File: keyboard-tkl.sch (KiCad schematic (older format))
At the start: 108 parts, among them P1 USB_OTG, P2 JTAG, U1 AT32UC3B1512, U2 74HC595, U3 74HC595, U4 74HC595, U5 LD1117S33CTR, Y1 12MHz

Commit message: Add stabs to big keys
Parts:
- added SW1, SW2, SW3, SW4, SW5, SW6: MX, mx1a:MXST, symbol MX
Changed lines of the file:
@@
 Wire Wire Line
 	10750 950  10750 1150
+$Comp
+L MX SW3
+U 1 1 55E28F84
+P 2450 2900
+F 0 "SW3" H 2450 2950 60  0000 C CNN
+F 1 "MX" H 2450 2850 60  0000 C CNN
+F 2 "mx1a:MXST" H 2450 2900 60  0000 C CNN
+F 3 "" H 2450 2900 60  0000 C CNN
+	1    2450 2900
+	1    0    0    -1
+$EndComp
+$Comp
+L MX SW4
+U 1 1 55E296F8
+P 4550 2900
+F 0 "SW4" H 4550 2950 60  0000 C CNN
+F 1 "MX" H 4550 2850 60  0000 C CNN
+F 2 "mx1a:MXST" H 4550 2900 60  0000 C CNN
+F 3 "" H 4550 2900 60  0000 C CNN
+	1    4550 2900
+	1    0    0    -1
+$EndComp
+$Comp
+L MX SW6
+U 1 1 55E29E84
+P 6150 2500
+F 0 "SW6" H 6150 2550 60  0000 C CNN
+F 1 "MX" H 6150 2450 60  0000 C CNN
+F 2 "mx1a:MXST" H 6150 2500 60  0000 C CNN
+F 3 "" H 6150 2500 60  0000 C CNN
+	1    6150 2500
+	1    0    0    -1
+$EndComp
+$Comp
+L MX SW5
+U 1 1 55E2A005
+P 5750 2500
+F 0 "SW5" H 5750 2550 60  0000 C CNN
+F 1 "MX" H 5750 2450 60  0000 C CNN
+F 2 "mx1a:MXST" H 5750 2500 60  0000 C CNN
+F 3 "" H 5750 2500 60  0000 C CNN
+	1    5750 2500
+	1    0    0    -1
+$EndComp
+$Comp
+L MX SW1
+U 1 1 55E2A3B8
+P 1150 2500
+F 0 "SW1" H 1150 2550 60  0000 C CNN
+F 1 "MX" H 1150 2450 60  0000 C CNN
+F 2 "mx1a:MXST" H 1150 2500 60  0000 C CNN
+F 3 "" H 1150 2500 60  0000 C CNN
+	1    1150 2500
+	1    0    0    -1
+$EndComp
+$Comp
+L MX SW2
+U 1 1 55E2A529
+P 1300 2500
+F 0 "SW2" H 1300 2550 60  0000 C CNN
+F 1 "MX" H 1300 2450 60  0000 C CNN
+F 2 "mx1a:MXST" H 1300 2500 60  0000 C CNN
+F 3 "" H 1300 2500 60  0000 C CNN
+	1    1300 2500
+	1    0    0    -1
+$EndComp
 $EndSCHEMATC

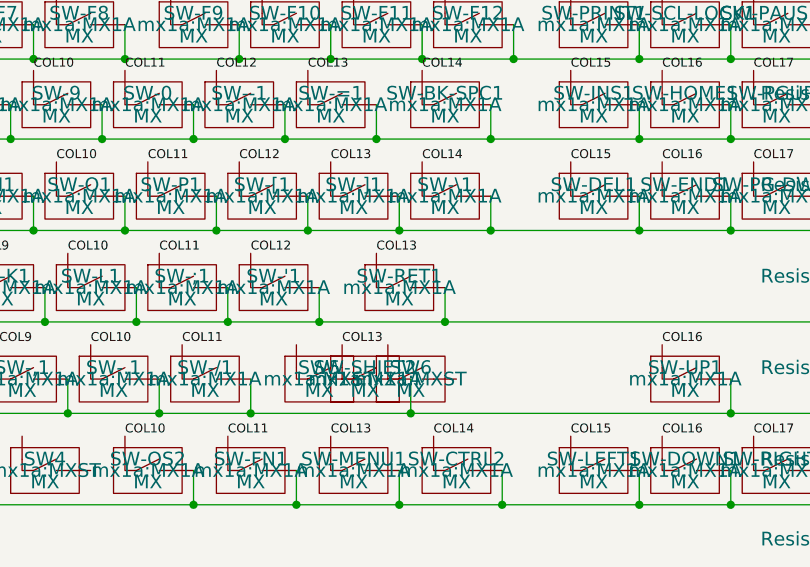
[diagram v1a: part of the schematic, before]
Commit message: Stabilizers placed and spaced
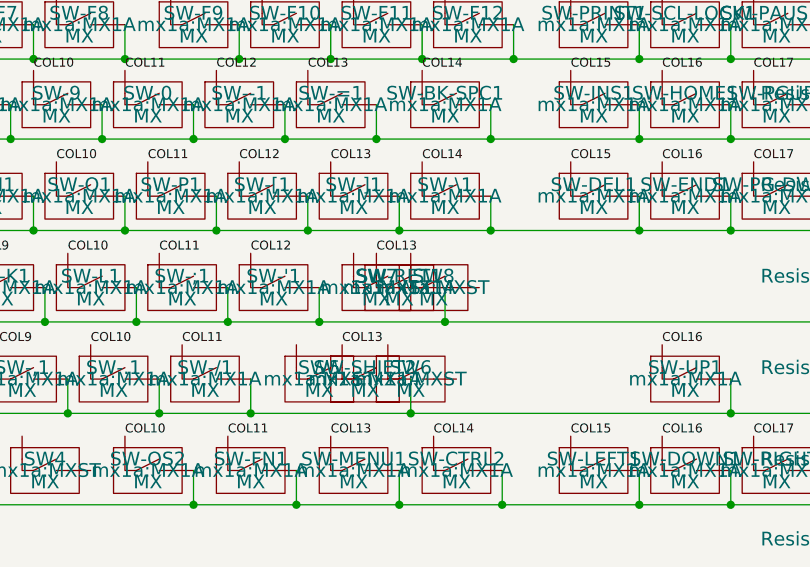
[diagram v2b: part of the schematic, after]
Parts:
- added SW7, SW8: MX, mx1a:MXST, symbol MX
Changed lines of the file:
@@
 $EndComp
 $Comp
-L +3.3V #PWR01
+L +3.3V #PWR2
 U 1 1 55DB292A
 P 2000 4150
-F 0 "#PWR01" H 2000 4000 50  0001 C CNN
+F 0 "#PWR2" H 2000 4000 50  0001 C CNN
 F 1 "+3.3V" H 2000 4290 50  0000 C CNN
 F 2 "" H 2000 4150 60  0000 C CNN
@@
 $EndComp
 $Comp
-L GND #PWR02
+L GND #PWR13
 U 1 1 55DC815B
 P 10800 6300
-F 0 "#PWR02" H 10800 6050 50  0001 C CNN
+F 0 "#PWR13" H 10800 6050 50  0001 C CNN
 F 1 "GND" H 10800 6150 50  0000 C CNN
 F 2 "" H 10800 6300 60  0000 C CNN
@@
 VDDOUT
 $Comp
-L GND #PWR03
+L GND #PWR16
 U 1 1 55DE1148
 P 12250 1450
-F 0 "#PWR03" H 12250 1200 50  0001 C CNN
+F 0 "#PWR16" H 12250 1200 50  0001 C CNN
 F 1 "GND" H 12250 1300 50  0000 C CNN
 F 2 "" H 12250 1450 60  0000 C CNN
@@
 $EndComp
 $Comp
-L +5V #PWR04
+L +5V #PWR15
 U 1 1 55DE1F1A
 P 11550 1400
-F 0 "#PWR04" H 11550 1250 50  0001 C CNN
+F 0 "#PWR15" H 11550 1250 50  0001 C CNN
 F 1 "+5V" H 11550 1540 50  0000 C CNN
 F 2 "" H 11550 1400 60  0000 C CNN
@@
 USB_ID
 $Comp
-L GND #PWR05
+L GND #PWR3
 U 1 1 55DEC1DC
 P 2200 8250
-F 0 "#PWR05" H 2200 8000 50  0001 C CNN
+F 0 "#PWR3" H 2200 8000 50  0001 C CNN
 F 1 "GND" H 2200 8100 50  0000 C CNN
 F 2 "" H 2200 8250 60  0000 C CNN
@@
 $EndComp
 $Comp
-L GND #PWR06
+L GND #PWR8
 U 1 1 55DF2FDE
 P 10050 6250
-F 0 "#PWR06" H 10050 6000 50  0001 C CNN
+F 0 "#PWR8" H 10050 6000 50  0001 C CNN
 F 1 "GND" H 10050 6100 50  0000 C CNN
 F 2 "" H 10050 6250 60  0000 C CNN
@@
 XOUT
 $Comp
-L +5V #PWR07
+L +5V #PWR1
 U 1 1 55DFF74B
 P 700 5250
-F 0 "#PWR07" H 700 5100 50  0001 C CNN
+F 0 "#PWR1" H 700 5100 50  0001 C CNN
 F 1 "+5V" H 700 5390 50  0000 C CNN
 F 2 "" H 700 5250 60  0000 C CNN
@@
 $EndComp
 $Comp
-L GND #PWR08
+L GND #PWR7
 U 1 1 55E14823
 P 9900 1350
-F 0 "#PWR08" H 9900 1100 50  0001 C CNN
+F 0 "#PWR7" H 9900 1100 50  0001 C CNN
 F 1 "GND" H 9900 1200 50  0000 C CNN
 F 2 "" H 9900 1350 60  0000 C CNN
@@
 $EndComp
 $Comp
-L +3.3V #PWR09
+L +3.3V #PWR9
 U 1 1 55E14901
 P 10350 950
-F 0 "#PWR09" H 10350 800 50  0001 C CNN
+F 0 "#PWR9" H 10350 800 50  0001 C CNN
 F 1 "+3.3V" H 10350 1090 50  0000 C CNN
 F 2 "" H 10350 950 60  0000 C CNN
@@
 $EndComp
 $Comp
-L +5V #PWR010
+L +5V #PWR6
 U 1 1 55E149DF
 P 9450 950
-F 0 "#PWR010" H 9450 800 50  0001 C CNN
+F 0 "#PWR6" H 9450 800 50  0001 C CNN
 F 1 "+5V" H 9450 1090 50  0000 C CNN
 F 2 "" H 9450 950 60  0000 C CNN
@@
 TMS
 $Comp
-L GND #PWR011
+L GND #PWR11
 U 1 1 55E1F92E
 P 10450 2750
-F 0 "#PWR011" H 10450 2500 50  0001 C CNN
+F 0 "#PWR11" H 10450 2500 50  0001 C CNN
 F 1 "GND" H 10450 2600 50  0000 C CNN
 F 2 "" H 10450 2750 60  0000 C CNN
@@
 $EndComp
 $Comp
-L +3.3V #PWR012
+L +3.3V #PWR10
 U 1 1 55E263FD
 P 10350 1950
-F 0 "#PWR012" H 10350 1800 50  0001 C CNN
+F 0 "#PWR10" H 10350 1800 50  0001 C CNN
 F 1 "+3.3V" H 10350 2090 50  0000 C CNN
 F 2 "" H 10350 1950 60  0000 C CNN
@@
 $EndComp
 $Comp
-L GND #PWR013
+L GND #PWR14
 U 1 1 55E2A264
 P 10950 2250
-F 0 "#PWR013" H 10950 2000 50  0001 C CNN
+F 0 "#PWR14" H 10950 2000 50  0001 C CNN
 F 1 "GND" H 10950 2100 50  0000 C CNN
 F 2 "" H 10950 2250 60  0000 C CNN
@@
 COL17
 $Comp
-L GND #PWR014
+L GND #PWR4
 U 1 1 55DAD7E2
 P 6150 4800
-F 0 "#PWR014" H 6150 4550 50  0001 C CNN
+F 0 "#PWR4" H 6150 4550 50  0001 C CNN
 F 1 "GND" H 6150 4650 50  0000 C CNN
 F 2 "" H 6150 4800 60  0000 C CNN
@@
 $EndComp
 $Comp
-L GND #PWR015
+L GND #PWR5
 U 1 1 55DBD0EC
 P 8350 3500
-F 0 "#PWR015" H 8350 3250 50  0001 C CNN
+F 0 "#PWR5" H 8350 3250 50  0001 C CNN
 F 1 "GND" H 8350 3350 50  0000 C CNN
 F 2 "" H 8350 3500 60  0000 C CNN
@@
 Connection ~ 8350 3300
 $Comp
-L +3.3V #PWR016
+L +3.3V #PWR12
 U 1 1 55DBEC7D
 P 10750 950
-F 0 "#PWR016" H 10750 800 50  0001 C CNN
+F 0 "#PWR12" H 10750 800 50  0001 C CNN
 F 1 "+3.3V" H 10750 1090 50  0000 C CNN
 F 2 "" H 10750 950 60  0000 C CNN
@@
 	1    0    0    -1
 $EndComp
+$Comp
+L MX SW8
+U 1 1 55E27F5A
+P 6250 2100
+F 0 "SW8" H 6250 2150 60  0000 C CNN
+F 1 "MX" H 6250 2050 60  0000 C CNN
+F 2 "mx1a:MXST" H 6250 2100 60  0000 C CNN
+F 3 "" H 6250 2100 60  0000 C CNN
+	1    6250 2100
+	1    0    0    -1
+$EndComp
+$Comp
+L MX SW7
+U 1 1 55E280C8
+P 6000 2100
+F 0 "SW7" H 6000 2150 60  0000 C CNN
+F 1 "MX" H 6000 2050 60  0000 C CNN
+F 2 "mx1a:MXST" H 6000 2100 60  0000 C CNN
+F 3 "" H 6000 2100 60  0000 C CNN
+	1    6000 2100
+	1    0    0    -1
+$EndComp

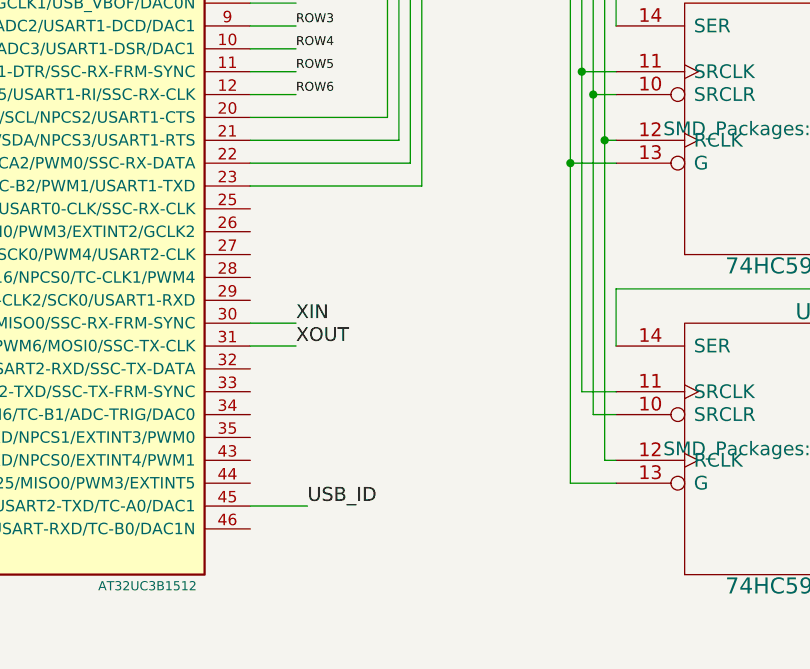
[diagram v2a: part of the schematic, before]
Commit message: Added status LEDs but they can't be driven by the micro.
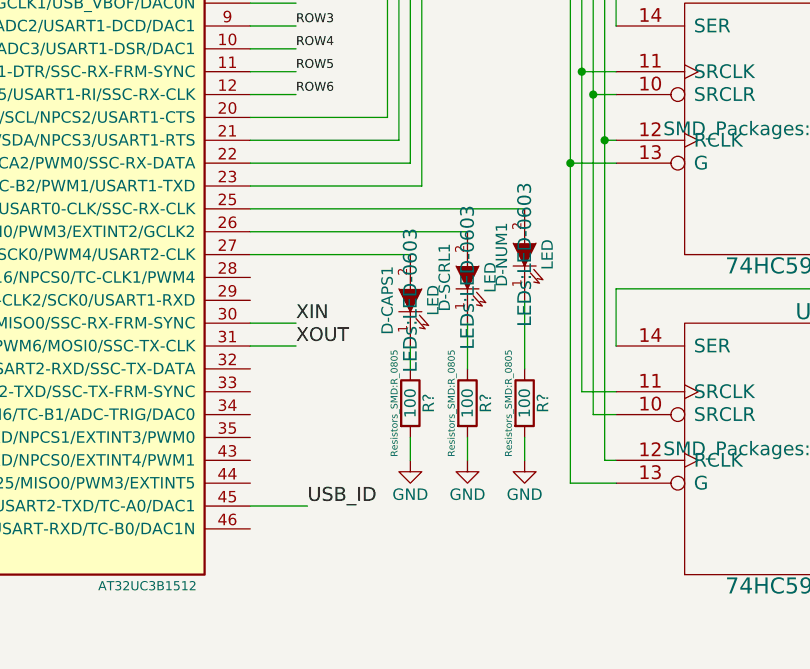
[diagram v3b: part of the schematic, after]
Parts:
- added D-CAPS1, D-NUM1, D-SCRL1: LED, LEDs:LED-0603, symbol LED
- added R? (x3): 100, Resistors_SMD:R_0805, symbol R
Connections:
- net GND: now also R?.2, R?.2, R?.2
- net at U1.25 (PA13/GPIO13/NMI/PWM2/USART0-CLK/SSC-RX-CLK): now also D-NUM1.2 (A)
- net at U1.26 (PA14/GPIO1/MOSI0/PWM3/EXTINT2/GCLK2): now also D-SCRL1.2 (A)
- net at U1.27 (PA15/GPIO15/SCK0/PWM4/USART2-CLK): now also D-CAPS1.2 (A)
- new net: D-NUM1.1 (K), R?.1
- new net: D-SCRL1.1 (K), R?.1
- new net: D-CAPS1.1 (K), R?.1
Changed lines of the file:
@@
 	1    0    0    -1
 $EndComp
+$Comp
+L LED D-NUM1
+U 1 1 55E29E33
+P 6250 6550
+F 0 "D-NUM1" H 6250 6650 50  0000 C CNN
+F 1 "LED" H 6250 6450 50  0000 C CNN
+F 2 "LEDs:LED-0603" H 6250 6550 60  0000 C CNN
+F 3 "" H 6250 6550 60  0000 C CNN
+F 4 "645-597-2903-507F" H 6250 6550 60  0001 C CNN "Mouser Part #"
+	1    6250 6550
+	0    -1   -1   0
+$EndComp
+$Comp
+L LED D-SCRL1
+U 1 1 55E2A000
+P 6000 6650
+F 0 "D-SCRL1" H 6000 6750 50  0000 C CNN
+F 1 "LED" H 6000 6550 50  0000 C CNN
+F 2 "LEDs:LED-0603" H 6000 6650 60  0000 C CNN
+F 3 "" H 6000 6650 60  0000 C CNN
+F 4 "645-597-2903-507F" H 6000 6650 60  0001 C CNN "Mouser Part #"
+	1    6000 6650
+	0    -1   -1   0
+$EndComp
+$Comp
+L LED D-CAPS1
+U 1 1 55E2A180
+P 5750 6750
+F 0 "D-CAPS1" H 5750 6850 50  0000 C CNN
+F 1 "LED" H 5750 6650 50  0000 C CNN
+F 2 "LEDs:LED-0603" H 5750 6750 60  0000 C CNN
+F 3 "" H 5750 6750 60  0000 C CNN
+F 4 "645-597-2903-507F" H 5750 6750 60  0001 C CNN "Mouser Part #"
+	1    5750 6750
+	0    -1   -1   0
+$EndComp
+Wire Wire Line
+	5050 6350 6250 6350
+Wire Wire Line
+	5050 6450 6000 6450
+Wire Wire Line
+	5050 6550 5750 6550
+$Comp
+L GND #PWR?
+U 1 1 55E2B688
+P 5750 7450
+F 0 "#PWR?" H 5750 7200 50  0001 C CNN
+F 1 "GND" H 5750 7300 50  0000 C CNN
+F 2 "" H 5750 7450 60  0000 C CNN
+F 3 "" H 5750 7450 60  0000 C CNN
+	1    5750 7450
+	1    0    0    -1
+$EndComp
+$Comp
+L GND #PWR?
+U 1 1 55E2CFAD
+P 6000 7450
+F 0 "#PWR?" H 6000 7200 50  0001 C CNN
+F 1 "GND" H 6000 7300 50  0000 C CNN
+F 2 "" H 6000 7450 60  0000 C CNN
+F 3 "" H 6000 7450 60  0000 C CNN
+	1    6000 7450
+	1    0    0    -1
+$EndComp
+$Comp
+L GND #PWR?
+U 1 1 55E2D11D
+P 6250 7450
+F 0 "#PWR?" H 6250 7200 50  0001 C CNN
+F 1 "GND" H 6250 7300 50  0000 C CNN
+F 2 "" H 6250 7450 60  0000 C CNN
+F 3 "" H 6250 7450 60  0000 C CNN
+	1    6250 7450
+	1    0    0    -1
+$EndComp
+$Comp
+L R R?
+U 1 1 55E2D3F4
+P 5750 7200
+F 0 "R?" V 5830 7200 50  0000 C CNN
+F 1 "100" V 5750 7200 50  0000 C CNN
+F 2 "Resistors_SMD:R_0805" V 5680 7200 30  0000 C CNN
+F 3 "" H 5750 7200 30  0000 C CNN
+	1    5750 7200
+	1    0    0    -1
+$EndComp
+$Comp
+L R R?
+U 1 1 55E2D57D
+P 6000 7200
+F 0 "R?" V 6080 7200 50  0000 C CNN
+F 1 "100" V 6000 7200 50  0000 C CNN
+F 2 "Resistors_SMD:R_0805" V 5930 7200 30  0000 C CNN
+F 3 "" H 6000 7200 30  0000 C CNN
+	1    6000 7200
+	1    0    0    -1
+$EndComp
+$Comp
+L R R?
+U 1 1 55E2D6FC
+P 6250 7200
+F 0 "R?" V 6330 7200 50  0000 C CNN
+F 1 "100" V 6250 7200 50  0000 C CNN
+F 2 "Resistors_SMD:R_0805" V 6180 7200 30  0000 C CNN
+F 3 "" H 6250 7200 30  0000 C CNN
+	1    6250 7200
+	1    0    0    -1
+$EndComp
+Wire Wire Line
+	5750 7350 5750 7450
+Wire Wire Line
+	6000 7350 6000 7450
+Wire Wire Line
+	6250 7350 6250 7450
+Wire Wire Line
+	6250 6750 6250 7050
+Wire Wire Line
+	6000 6850 6000 7050
+Wire Wire Line
+	5750 6950 5750 7050
 $EndSCHEMATC

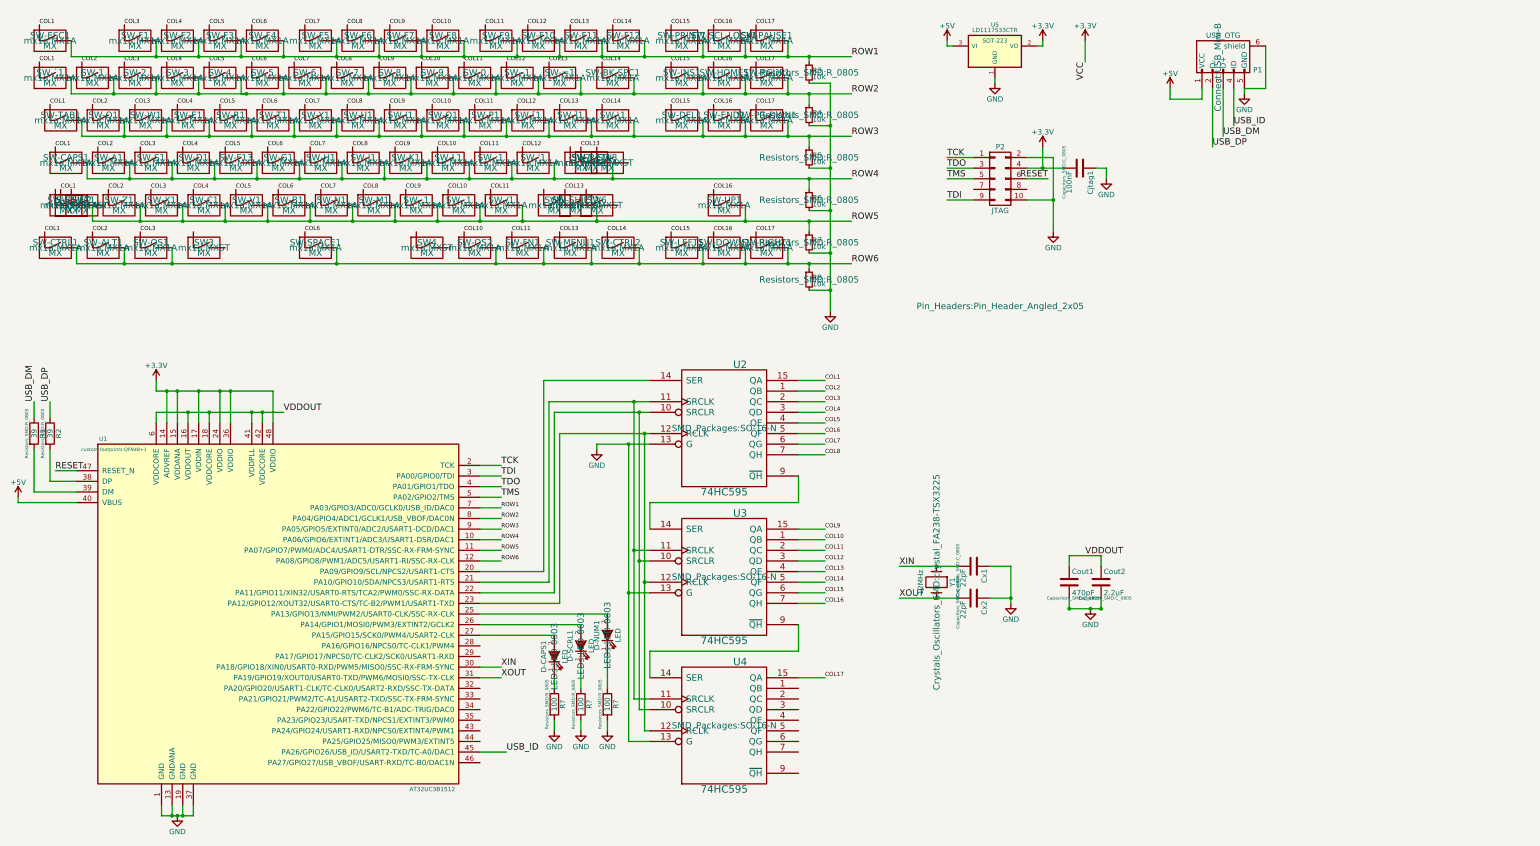
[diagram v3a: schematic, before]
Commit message: LEDs added, but not placed
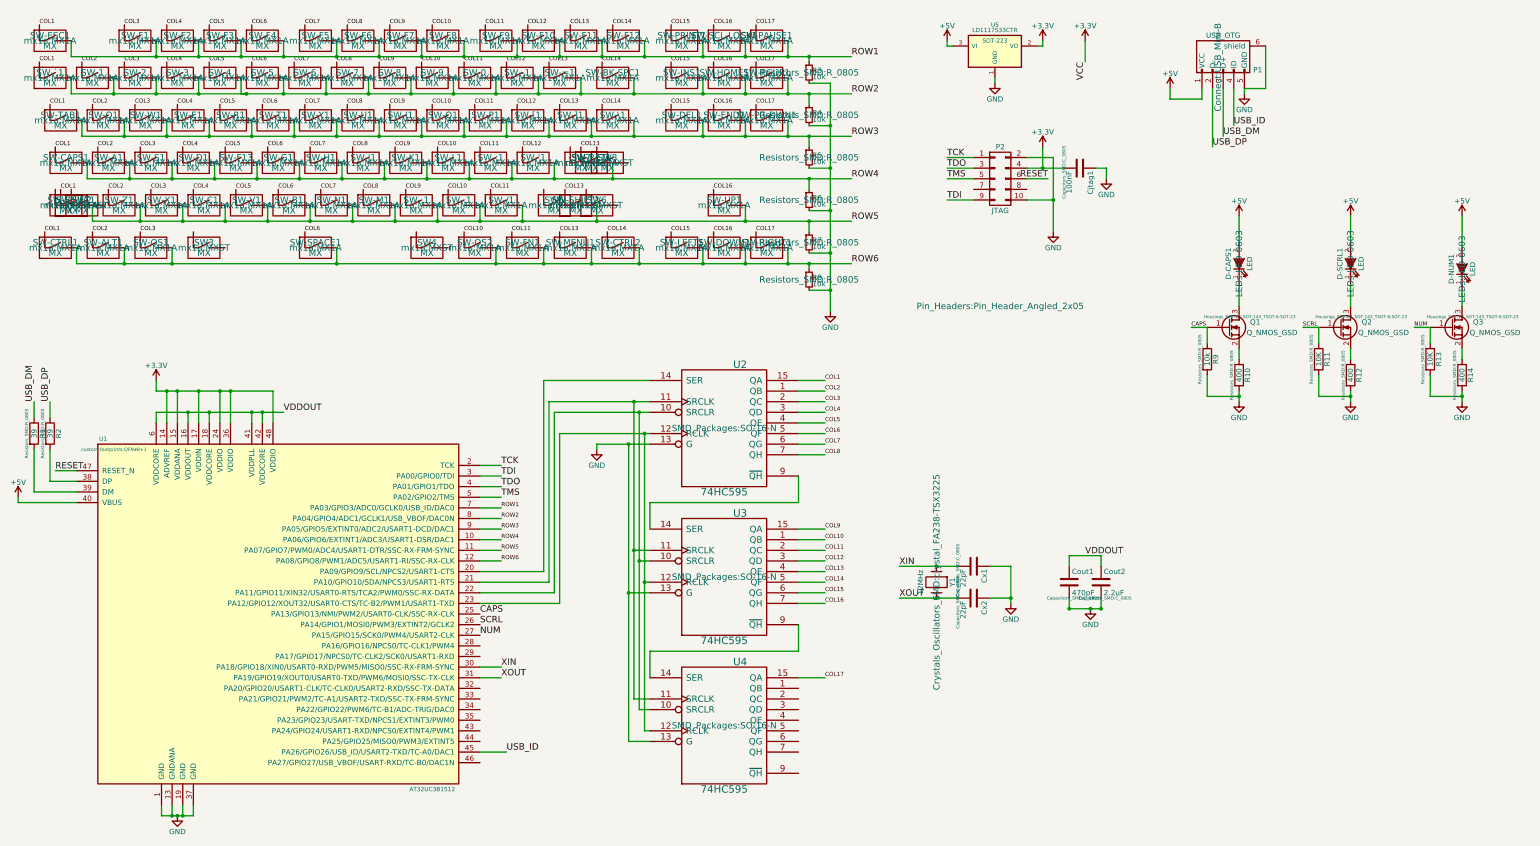
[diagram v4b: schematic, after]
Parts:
- removed R? (x3): 100, Resistors_SMD:R_0805, symbol R
- added Q1, Q2, Q3: Q_NMOS_GSD, Housings_SOT-23_SOT-143_TSOT-6:SOT-23, symbol Q_NMOS_GSD
- added R10, R12, R14: 400, Resistors_SMD:R_0805, symbol R
- added R11, R13: 10K, Resistors_SMD:R_0805, symbol R
- added R9: 10k, Resistors_SMD:R_0805, symbol R
- D-CAPS1, D-NUM1, D-SCRL1: Mouser Part # 645-597-2903-507F -> 630-ASMT-CW00
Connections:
- net +5V: now also D-CAPS1.2 (A), D-NUM1.2 (A), D-SCRL1.2 (A)
- net GND: now also R10.2, R11.2, R12.2, R13.2, R14.2, R9.2
- net CAPS: now reaches U1.25 (PA13/GPIO13/NMI/PWM2/USART0-CLK/SSC-RX-CLK)
- net CAPS: now also Q1.1 (G), R9.1; no longer D-NUM1.2 (A)
- net SCRL: now reaches U1.26 (PA14/GPIO1/MOSI0/PWM3/EXTINT2/GCLK2)
- net SCRL: now also Q2.1 (G), R11.1; no longer D-SCRL1.2 (A)
- net NUM: now reaches U1.27 (PA15/GPIO15/SCK0/PWM4/USART2-CLK)
- net NUM: now also Q3.1 (G), R13.1; no longer D-CAPS1.2 (A)
- net at D-NUM1.1 (K): now also Q3.3 (D)
- net at D-SCRL1.1 (K): now also Q2.3 (D)
- net at D-CAPS1.1 (K): now also Q1.3 (D)
- new net: Q1.2 (S), R10.1
- new net: Q2.2 (S), R12.1
- new net: Q3.2 (S), R14.1
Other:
- moved on the sheet: D-CAPS1, D-NUM1, D-SCRL1
